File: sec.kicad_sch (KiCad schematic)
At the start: 0 parts

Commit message: finishing the sec shematic
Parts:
- added U3, U6: 4510, symbol 4xxx:4510
- added U4, U5: 4081, symbol 4xxx:4081
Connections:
- new net: U3.9 (RST), U5.3, U6.15 (CLK)
- new net +5V: U3.10 (U/D), U3.16 (VDD), U4.14 (VDD), U6.10 (U/D), U6.16 (VDD)
- new net CLK: U3.15 (CLK)
- new net GND: U3.1 (PE), U3.12 (A2), U3.13 (A3), U3.3 (A4), U3.4 (A1), U3.5 (CI), U3.8 (VSS), U4.10, U4.12, U4.13, U4.7 (VSS), U4.8, U4.9, U6.1 (PE), U6.12 (A2), U6.13 (A3), U6.3 (A4), U6.4 (A1), U6.5 (CI), U6.8 (VSS)
- new net min_clk: U4.4, U6.9 (RST)
- new net sec-o_1: U3.6 (Q1)
- new net sec-o_2: U3.11 (Q2), U5.1
- new net sec-o_3: U3.14 (Q3)
- new net sec-o_4: U3.2 (Q4), U5.2
- new net sec-t_1: U6.6 (Q1)
- new net sec-t_2: U4.5, U6.11 (Q2)
- new net sec-t_3: U4.6, U6.14 (Q3)
- new net sec-t_4: U6.2 (Q4)

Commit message: adding the time seting buttons
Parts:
- removed unit 3 of U4
- removed unit 4 of U4
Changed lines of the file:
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@@
-	)
-	(symbol
-		(lib_id "4xxx:4081")
-		(at 34.29 129.54 0)
-		(unit 3)
-		(body_style 1)
-		(exclude_from_sim no)
-		(in_bom yes)
-		(on_board yes)
-		(in_pos_files yes)
-		(dnp no)
-		(fields_autoplaced yes)
-		(property "Reference" "U4"
-			(at 34.2817 120.65 0)
-			(show_name no)
-			(do_not_autoplace no)
-			(effects
-				(font
-					(size 1.27 1.27)
-				)
-			)
-		)
-		(property "Value" "4081"
-			(at 34.2817 123.19 0)
-			(show_name no)
-			(do_not_autoplace no)
-			(effects
-				(font
-					(size 1.27 1.27)
-				)
-			)
-		)
-		(property "Footprint" ""
-			(at 34.29 129.54 0)
-			(hide yes)
-			(show_name no)
-			(do_not_autoplace no)
-			(effects
-				(font
-					(size 1.27 1.27)
-				)
-			)
-		)
-		(property "Datasheet" "http://www.intersil.com/content/dam/Intersil/documents/cd40/cd4073bms-81bms-82bms.pdf"
-			(at 34.29 129.54 0)
-			(hide yes)
-			(show_name no)
-			(do_not_autoplace no)
-			(effects
-				(font
-					(size 1.27 1.27)
-				)
-			)
-		)
-		(property "Description" "Quad And 2 inputs"
-			(at 34.29 129.54 0)
-			(hide yes)
-			(show_name no)
-			(do_not_autoplace no)
-			(effects
-				(font
-					(size 1.27 1.27)
-				)
-			)
-		)
-		(pin "4"
-		)
-		(pin "6"
-		)
-		(pin "1"
-		)
-		(pin "13"
-		)
-		(pin "14"
-		)
-		(pin "8"
-		)
-		(pin "10"
-		)
-		(pin "9"
-		)
-		(pin "3"
-		)
-		(pin "2"
-		)
-		(pin "5"
-		)
-		(pin "7"
-		)
-		(pin "11"
-		)
-		(pin "12"
-		)
-		(instances
-			(project "BinaryClock"
-				(path "/b8db7867-2c41-4996-89b7-85623a375f4b/d72dbc43-5f9c-4389-b46b-bcc9f20f0691/02494b62-5cd5-41fe-b50f-3d6e2444706b"
-					(reference "U4")
-					(unit 3)
-				)
-			)
-		)
 	)
 	(symbol
@@
 				)
 			)
-		)
-	)
-	(symbol
-		(lib_id "4xxx:4081")
-		(at 34.29 140.97 0)
-		(unit 4)
-		(body_style 1)
-		(exclude_from_sim no)
-		(in_bom yes)
-		(on_board yes)
-		(in_pos_files yes)
-		(dnp no)
-		(fields_autoplaced yes)
-		(property "Reference" "U4"
-			(at 34.2817 132.08 0)
-			(show_name no)
-			(do_not_autoplace no)
-			(effects
-				(font
-					(size 1.27 1.27)
-				)
-			)
-		)
-		(property "Value" "4081"
-			(at 34.2817 134.62 0)
-			(show_name no)
-			(do_not_autoplace no)
-			(effects
-				(font
-					(size 1.27 1.27)
-				)
-			)
-		)
-		(property "Footprint" ""
-			(at 34.29 140.97 0)
-			(hide yes)
-			(show_name no)
-			(do_not_autoplace no)
-			(effects
-				(font
-					(size 1.27 1.27)
-				)
-			)
-		)
-		(property "Datasheet" "http://www.intersil.com/content/dam/Intersil/documents/cd40/cd4073bms-81bms-82bms.pdf"
-			(at 34.29 140.97 0)
-			(hide yes)
-			(show_name no)
-			(do_not_autoplace no)
-			(effects
-				(font
-					(size 1.27 1.27)
-				)
-			)
-		)
-		(property "Description" "Quad And 2 inputs"
-			(at 34.29 140.97 0)
-			(hide yes)
-			(show_name no)
-			(do_not_autoplace no)
-			(effects
-				(font
-					(size 1.27 1.27)
-				)
-			)
-		)
-		(pin "4"
-		)
-		(pin "6"
-		)
-		(pin "1"
-		)
-		(pin "13"
-		)
-		(pin "14"
-		)
-		(pin "8"
-		)
-		(pin "10"
-		)
-		(pin "9"
-		)
-		(pin "3"
-		)
-		(pin "2"
-		)
-		(pin "5"
-		)
-		(pin "7"
-		)
-		(pin "11"
-		)
-		(pin "12"
-		)
-		(instances
-			(project "BinaryClock"
-				(path "/b8db7867-2c41-4996-89b7-85623a375f4b/d72dbc43-5f9c-4389-b46b-bcc9f20f0691/02494b62-5cd5-41fe-b50f-3d6e2444706b"
-					(reference "U4")
-					(unit 4)
-				)
-			)

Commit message: Making the circuit for the hour counter
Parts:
- removed U5: 4081, symbol 4xxx:4081
- added unit 1 of U3
- renumbered U4 to U3, U3 to U4, U6 to U5
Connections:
- net sec-o_2: now also U3.1
- net sec-o_4: now also U3.2
- net at U4.9 (RST), U5.15 (CLK): now also U3.3
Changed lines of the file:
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@@
 		(dnp no)
 		(fields_autoplaced yes)
-		(property "Reference" "#PWR021"
+		(property "Reference" "#PWR019"
 			(at 66.04 77.47 0)
 			(hide yes)
@@
 			(project "BinaryClock"
 				(path "/b8db7867-2c41-4996-89b7-85623a375f4b/d72dbc43-5f9c-4389-b46b-bcc9f20f0691/02494b62-5cd5-41fe-b50f-3d6e2444706b"
-					(reference "#PWR021")
+					(reference "#PWR019")
 					(unit 1)
 				)
@@
 		(dnp no)
 		(fields_autoplaced yes)
-		(property "Reference" "#PWR019"
+		(property "Reference" "#PWR017"
 			(at 66.04 72.39 0)
 			(hide yes)
@@
 			(project "BinaryClock"
 				(path "/b8db7867-2c41-4996-89b7-85623a375f4b/d72dbc43-5f9c-4389-b46b-bcc9f20f0691/02494b62-5cd5-41fe-b50f-3d6e2444706b"
-					(reference "#PWR019")
-					(unit 1)
-				)
-			)
-		)
-	)
-	(symbol
-		(lib_id "4xxx:4081")
-		(at 124.46 74.93 0)
-		(unit 1)
-		(body_style 1)
-		(exclude_from_sim no)
-		(in_bom yes)
-		(on_board yes)
-		(in_pos_files yes)
-		(dnp no)
-		(fields_autoplaced yes)
-		(property "Reference" "U5"
-			(at 124.4517 66.04 0)
-			(show_name no)
-			(do_not_autoplace no)
-			(effects
-				(font
-					(size 1.27 1.27)
-				)
-			)
-		)
-		(property "Value" "4081"
-			(at 124.4517 68.58 0)
-			(show_name no)
-			(do_not_autoplace no)
-			(effects
-				(font
-					(size 1.27 1.27)
-				)
-			)
-		)
-		(property "Footprint" ""
-			(at 124.46 74.93 0)
-			(hide yes)
-			(show_name no)
-			(do_not_autoplace no)
-			(effects
-				(font
-					(size 1.27 1.27)
-				)
-			)
-		)
-		(property "Datasheet" "http://www.intersil.com/content/dam/Intersil/documents/cd40/cd4073bms-81bms-82bms.pdf"
-			(at 124.46 74.93 0)
-			(hide yes)
-			(show_name no)
-			(do_not_autoplace no)
-			(effects
-				(font
-					(size 1.27 1.27)
-				)
-			)
-		)
-		(property "Description" "Quad And 2 inputs"
-			(at 124.46 74.93 0)
-			(hide yes)
-			(show_name no)
-			(do_not_autoplace no)
-			(effects
-				(font
-					(size 1.27 1.27)
-				)
-			)
-		)
-		(pin "4"
-		)
-		(pin "6"
-		)
-		(pin "1"
-		)
-		(pin "13"
-		)
-		(pin "14"
-		)
-		(pin "8"
-		)
-		(pin "10"
-		)
-		(pin "9"
-		)
-		(pin "3"
-		)
-		(pin "2"
-		)
-		(pin "5"
-		)
-		(pin "7"
-		)
-		(pin "11"
-		)
-		(pin "12"
-		)
-		(instances
-			(project "BinaryClock"
-				(path "/b8db7867-2c41-4996-89b7-85623a375f4b/d72dbc43-5f9c-4389-b46b-bcc9f20f0691/02494b62-5cd5-41fe-b50f-3d6e2444706b"
-					(reference "U5")
+					(reference "#PWR017")
 					(unit 1)
 				)
@@
 		(dnp no)
 		(fields_autoplaced yes)
-		(property "Reference" "#PWR016"
+		(property "Reference" "#PWR021"
 			(at 76.2 85.09 0)
 			(hide yes)
@@
 			(project "BinaryClock"
 				(path "/b8db7867-2c41-4996-89b7-85623a375f4b/d72dbc43-5f9c-4389-b46b-bcc9f20f0691/02494b62-5cd5-41fe-b50f-3d6e2444706b"
-					(reference "#PWR016")
+					(reference "#PWR021")
 					(unit 1)
 				)
@@
 		(dnp no)
 		(fields_autoplaced yes)
-		(property "Reference" "#PWR014"
+		(property "Reference" "#PWR023"
 			(at 85.09 66.04 0)
 			(hide yes)
@@
 			(project "BinaryClock"
 				(path "/b8db7867-2c41-4996-89b7-85623a375f4b/d72dbc43-5f9c-4389-b46b-bcc9f20f0691/02494b62-5cd5-41fe-b50f-3d6e2444706b"
-					(reference "#PWR014")
+					(reference "#PWR023")
 					(unit 1)
 				)
@@
 		(dnp no)
 		(fields_autoplaced yes)
-		(property "Reference" "#PWR020"
+		(property "Reference" "#PWR018"
 			(at 66.04 74.93 0)
 			(hide yes)
@@
 			(project "BinaryClock"
 				(path "/b8db7867-2c41-4996-89b7-85623a375f4b/d72dbc43-5f9c-4389-b46b-bcc9f20f0691/02494b62-5cd5-41fe-b50f-3d6e2444706b"
-					(reference "#PWR020")
+					(reference "#PWR018")
 					(unit 1)
 				)
@@
 		(dnp no)
 		(fields_autoplaced yes)
-		(property "Reference" "U4"
+		(property "Reference" "U3"
 			(at 218.4317 54.61 0)
 			(show_name no)
@@
 			(project "BinaryClock"
 				(path "/b8db7867-2c41-4996-89b7-85623a375f4b/d72dbc43-5f9c-4389-b46b-bcc9f20f0691/02494b62-5cd5-41fe-b50f-3d6e2444706b"
-					(reference "U4")
+					(reference "U3")
 					(unit 2)
 				)
@@
 		(dnp no)
 		(fields_autoplaced yes)
-		(property "Reference" "U6"
+		(property "Reference" "U5"
 			(at 181.2133 53.34 0)
 			(show_name no)
@@
 			(project "BinaryClock"
 				(path "/b8db7867-2c41-4996-89b7-85623a375f4b/d72dbc43-5f9c-4389-b46b-bcc9f20f0691/02494b62-5cd5-41fe-b50f-3d6e2444706b"
-					(reference "U6")
+					(reference "U5")
 					(unit 1)
 				)
@@
 		(dnp no)
 		(fields_autoplaced yes)
-		(property "Reference" "#PWR018"
+		(property "Reference" "#PWR016"
 			(at 66.04 69.85 0)
 			(hide yes)
@@
 			(project "BinaryClock"
 				(path "/b8db7867-2c41-4996-89b7-85623a375f4b/d72dbc43-5f9c-4389-b46b-bcc9f20f0691/02494b62-5cd5-41fe-b50f-3d6e2444706b"
-					(reference "#PWR018")
+					(reference "#PWR016")
 					(unit 1)
 				)
@@
 		(dnp no)
 		(fields_autoplaced yes)
-		(property "Reference" "#PWR023"
+		(property "Reference" "#PWR014"
 			(at 50.8 165.1 0)
 			(hide yes)
@@
 			(project "BinaryClock"
 				(path "/b8db7867-2c41-4996-89b7-85623a375f4b/d72dbc43-5f9c-4389-b46b-bcc9f20f0691/02494b62-5cd5-41fe-b50f-3d6e2444706b"
-					(reference "#PWR023")
+					(reference "#PWR014")
 					(unit 1)
 				)
@@
 		(dnp no)
 		(fields_autoplaced yes)
-		(property "Reference" "#PWR022"
+		(property "Reference" "#PWR020"
 			(at 66.04 82.55 0)
 			(hide yes)
@@
 			(project "BinaryClock"
 				(path "/b8db7867-2c41-4996-89b7-85623a375f4b/d72dbc43-5f9c-4389-b46b-bcc9f20f0691/02494b62-5cd5-41fe-b50f-3d6e2444706b"
-					(reference "#PWR022")
+					(reference "#PWR020")
 					(unit 1)
 				)
@@
 		(dnp no)
 		(fields_autoplaced yes)
-		(property "Reference" "#PWR024"
+		(property "Reference" "#PWR015"
 			(at 50.8 193.04 0)
 			(hide yes)
@@
 			(project "BinaryClock"
 				(path "/b8db7867-2c41-4996-89b7-85623a375f4b/d72dbc43-5f9c-4389-b46b-bcc9f20f0691/02494b62-5cd5-41fe-b50f-3d6e2444706b"
-					(reference "#PWR024")
+					(reference "#PWR015")
 					(unit 1)
 				)
@@
 		(dnp no)
 		(fields_autoplaced yes)
-		(property "Reference" "#PWR015"
+		(property "Reference" "#PWR024"
 			(at 85.09 106.68 0)
 			(hide yes)
@@
 			(project "BinaryClock"
 				(path "/b8db7867-2c41-4996-89b7-85623a375f4b/d72dbc43-5f9c-4389-b46b-bcc9f20f0691/02494b62-5cd5-41fe-b50f-3d6e2444706b"
-					(reference "#PWR015")
+					(reference "#PWR024")
 					(unit 1)
 				)
@@
 		(dnp no)
 		(fields_autoplaced yes)
-		(property "Reference" "U3"
+		(property "Reference" "U4"
 			(at 87.2333 62.23 0)
 			(show_name no)
@@
 		)
 		(pin "9"
+		)
+		(instances
+			(project "BinaryClock"
+				(path "/b8db7867-2c41-4996-89b7-85623a375f4b/d72dbc43-5f9c-4389-b46b-bcc9f20f0691/02494b62-5cd5-41fe-b50f-3d6e2444706b"
+					(reference "U4")
+					(unit 1)
+				)
+			)
+		)
+	)
+	(symbol
+		(lib_id "4xxx:4081")
+		(at 124.46 74.93 0)
+		(unit 1)
+		(body_style 1)
+		(exclude_from_sim no)
+		(in_bom yes)
+		(on_board yes)
+		(in_pos_files yes)
+		(dnp no)
+		(fields_autoplaced yes)
+		(property "Reference" "U3"
+			(at 124.4517 66.04 0)
+			(show_name no)
+			(do_not_autoplace no)
+			(effects
+				(font
+					(size 1.27 1.27)
+				)
+			)
+		)
+		(property "Value" "4081"
+			(at 124.4517 68.58 0)
+			(show_name no)
+			(do_not_autoplace no)
+			(effects
+				(font
+					(size 1.27 1.27)
+				)
+			)
+		)
+		(property "Footprint" "Package_DIP:DIP-14_W7.62mm_Socket_LongPads"
+			(at 124.46 74.93 0)
+			(hide yes)
+			(show_name no)
+			(do_not_autoplace no)
+			(effects
+				(font
+					(size 1.27 1.27)
+				)
+			)
+		)
+		(property "Datasheet" "http://www.intersil.com/content/dam/Intersil/documents/cd40/cd4073bms-81bms-82bms.pdf"
+			(at 124.46 74.93 0)
+			(hide yes)
+			(show_name no)
+			(do_not_autoplace no)
+			(effects
+				(font
+					(size 1.27 1.27)
+				)
+			)
+		)
+		(property "Description" "Quad And 2 inputs"
+			(at 124.46 74.93 0)
+			(hide yes)
+			(show_name no)
+			(do_not_autoplace no)
+			(effects
+				(font
+					(size 1.27 1.27)
+				)
+			)
+		)
+		(pin "13"
+		)
+		(pin "14"
+		)
+		(pin "5"
+		)
+		(pin "9"
+		)
+		(pin "11"
+		)
+		(pin "10"
+		)
+		(pin "8"
+		)
+		(pin "7"
+		)
+		(pin "4"
+		)
+		(pin "3"
+		)
+		(pin "2"
+		)
+		(pin "1"
+		)
+		(pin "6"
+		)
+		(pin "12"
 		)
 		(instances
@@
 		(dnp no)
 		(fields_autoplaced yes)
-		(property "Reference" "U4"
+		(property "Reference" "U3"
 			(at 57.15 172.7199 0)
 			(show_name no)
@@
 			(project "BinaryClock"
 				(path "/b8db7867-2c41-4996-89b7-85623a375f4b/d72dbc43-5f9c-4389-b46b-bcc9f20f0691/02494b62-5cd5-41fe-b50f-3d6e2444706b"
-					(reference "U4")
+					(reference "U3")
 					(unit 5)
 				)
@@
 		(dnp no)
 		(fields_autoplaced yes)
-		(property "Reference" "#PWR017"
+		(property "Reference" "#PWR022"
 			(at 66.04 90.17 0)
 			(hide yes)
@@
 			(project "BinaryClock"
 				(path "/b8db7867-2c41-4996-89b7-85623a375f4b/d72dbc43-5f9c-4389-b46b-bcc9f20f0691/02494b62-5cd5-41fe-b50f-3d6e2444706b"
-					(reference "#PWR017")
-					(unit 1)
-				)
+					(reference "#PWR022")
+					(unit 1)
+				)

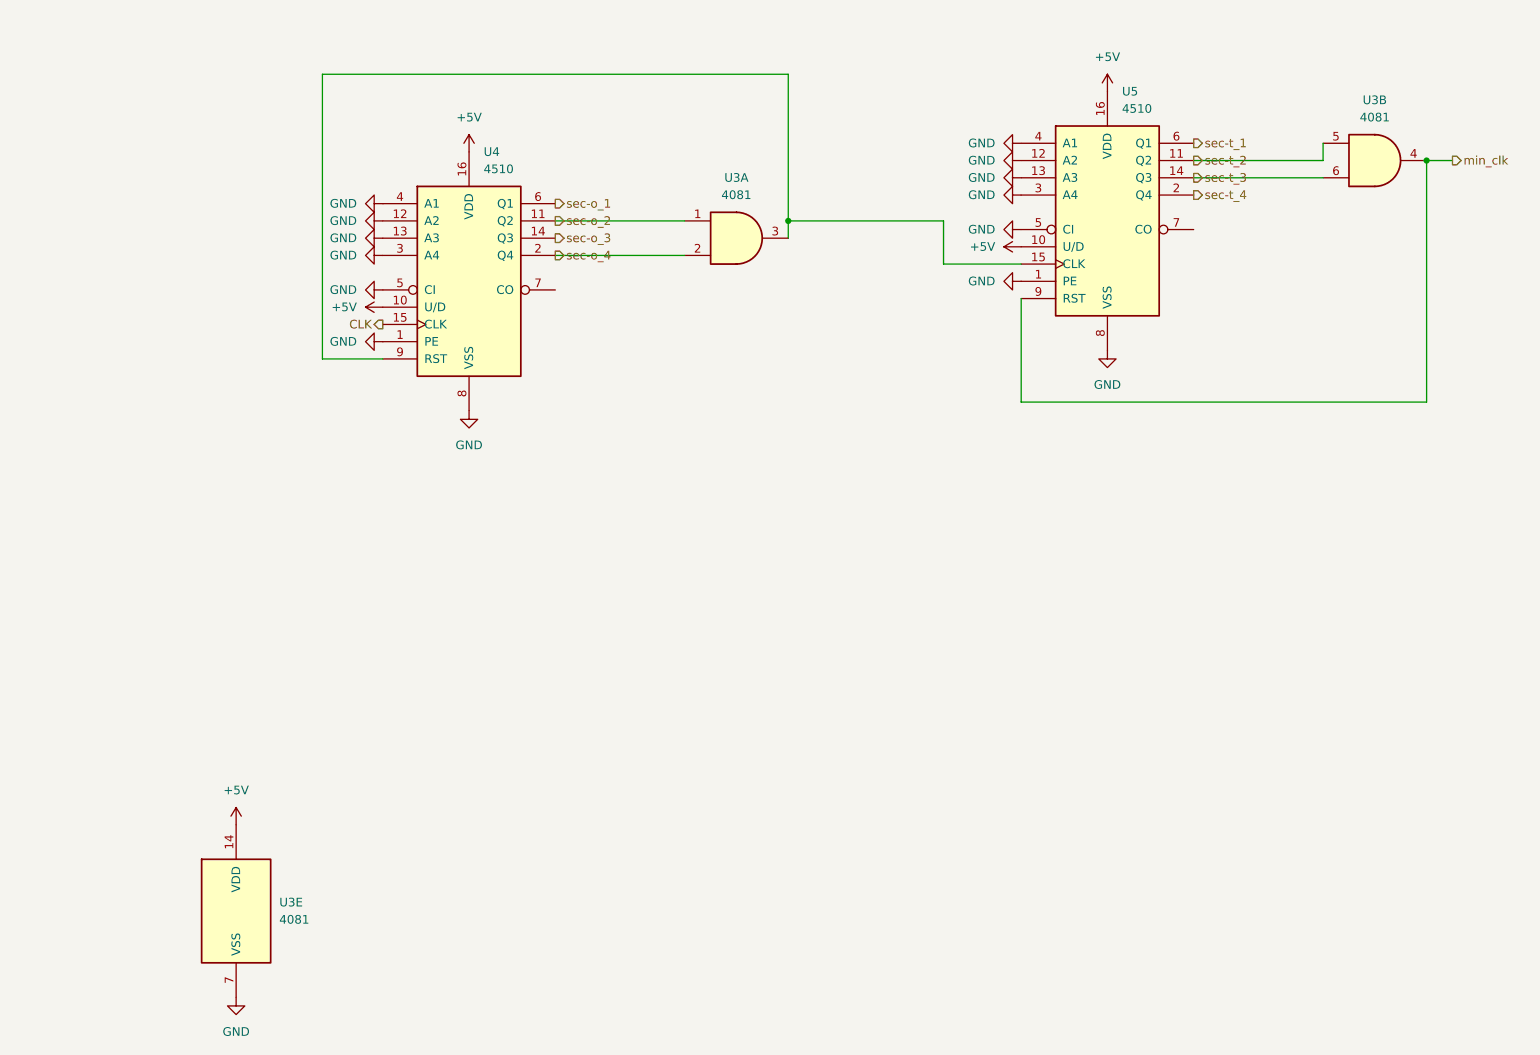
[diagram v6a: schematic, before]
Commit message: Making the 24 rst for ewery counter and adding Capacitors
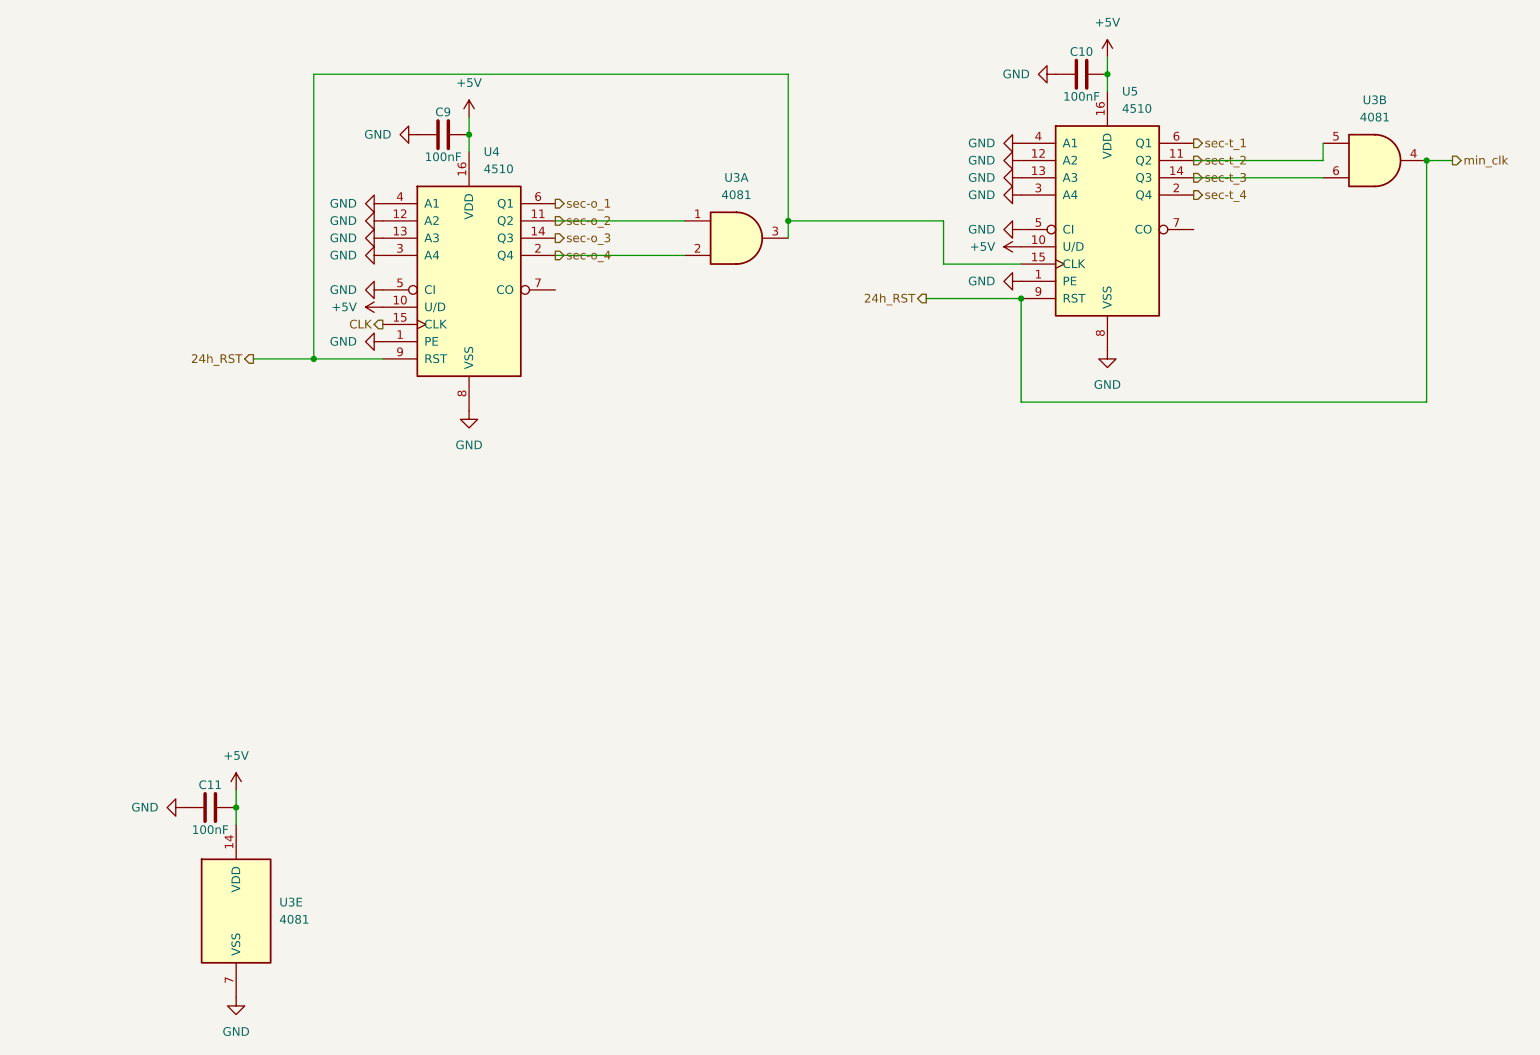
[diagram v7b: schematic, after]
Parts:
- added C10, C11, C9: 100nF, symbol Device:C
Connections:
- net min_clk is gone; now on net 24h_RST: U3.4, U5.9 (RST)
- net +5V: now also C10.2, C11.2, C9.2
- net GND: now also C10.1, C11.1, C9.1
- net 24h_RST: now reaches U3.3, U4.9 (RST), U5.15 (CLK)
